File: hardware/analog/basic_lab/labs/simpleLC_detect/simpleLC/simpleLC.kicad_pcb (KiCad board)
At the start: 2 copper layers, 36.2 x 15 mm, 5 parts, among them J1 Conn_01x04_Male, J2 Conn_01x02_Male, Q2 BC547

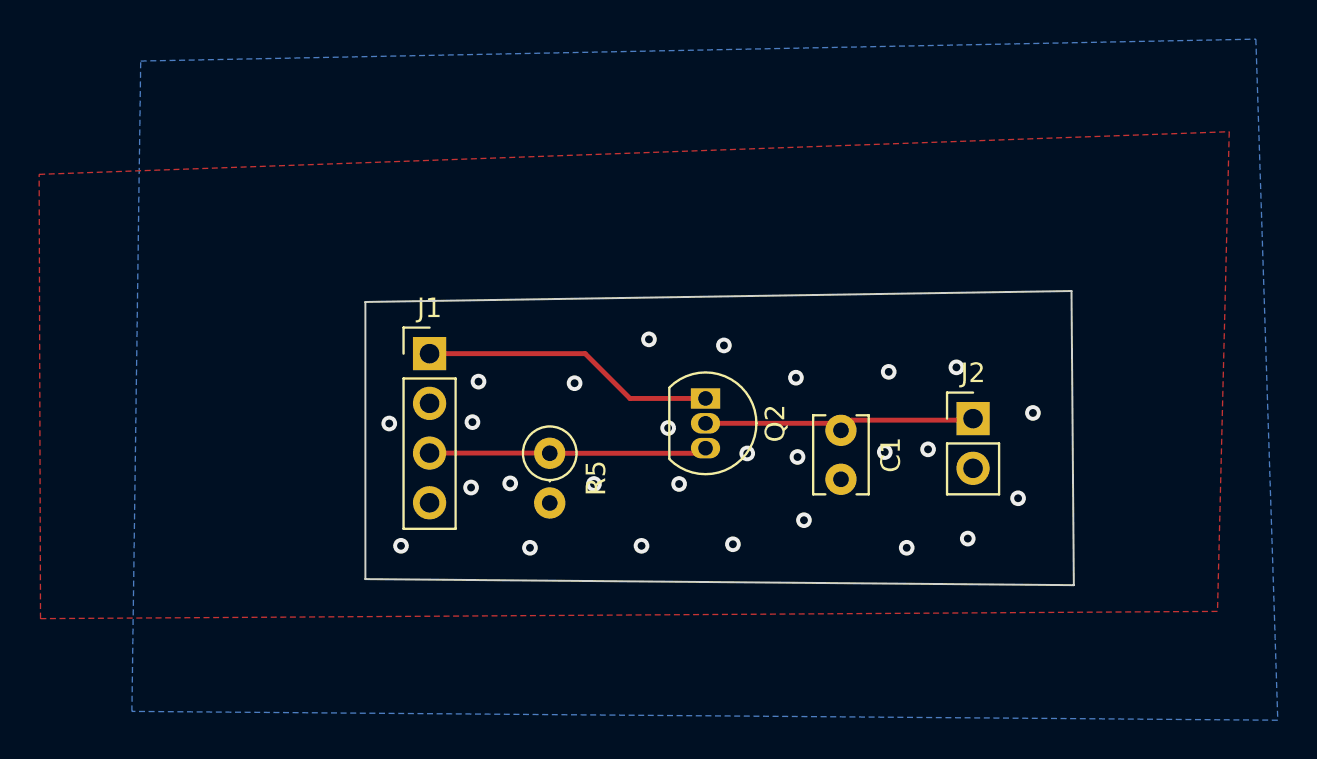
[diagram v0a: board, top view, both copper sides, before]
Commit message: PWM => detect / flyback
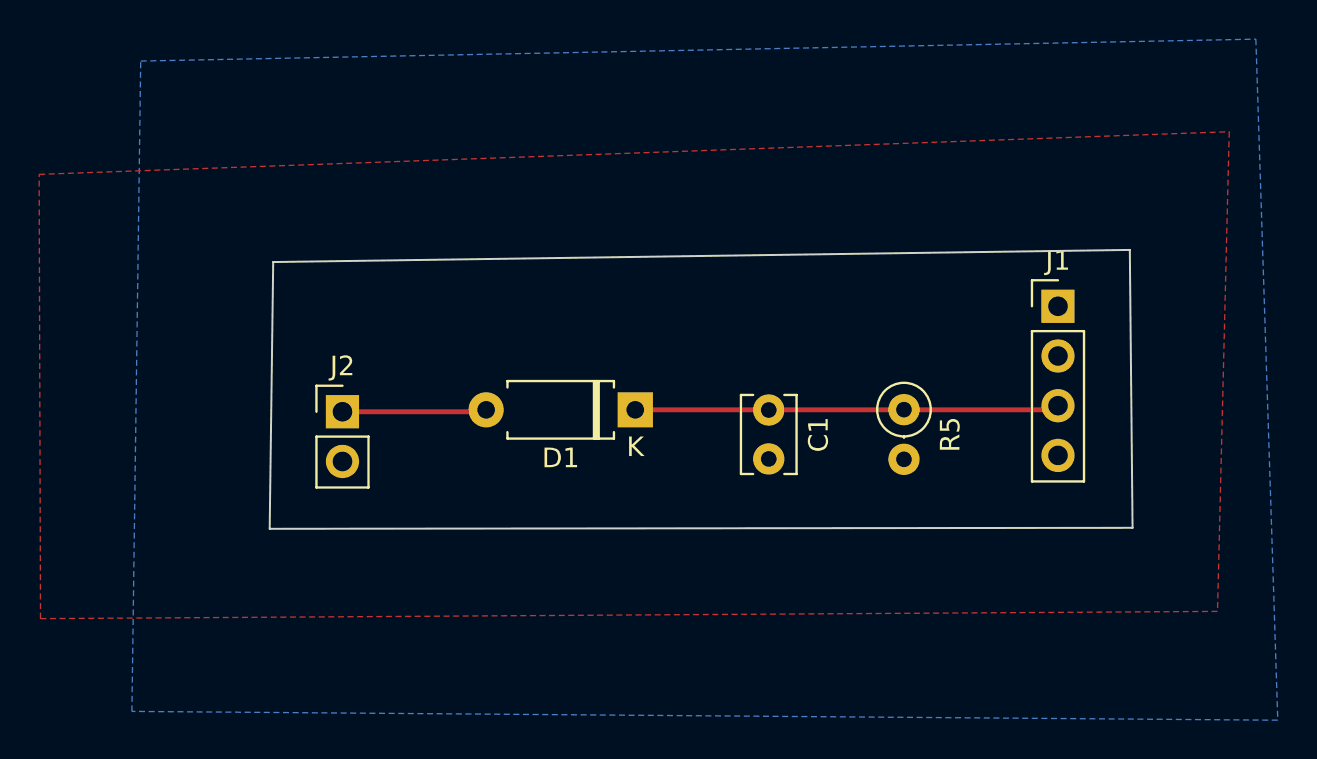
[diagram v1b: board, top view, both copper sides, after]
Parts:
- removed Q2: BC547, Package_TO_SOT_THT:TO-92_Inline
- added D1: D, Diode_THT:D_A-405_P7.62mm_Horizontal, F.Cu at (177.4, 92.5)
- moved J2 32.2 mm to (162.5, 92.7)
- moved J1 32.2 mm to (199.0, 87.3)
- moved R5 18.2 mm to (191.2, 92.5)
- moved C1 3.83 mm to (184.2, 92.6)
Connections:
- C1 pad 1: Net-(C1-Pad1) -> aout
- J2 pad 1: Net-(C1-Pad1) -> Net-(D1-Pad2)
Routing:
- net +3V3: track 15.0 -> 0.00 mm
- net Net-(C1-Pad1): track 14.0 -> 0.00 mm
- net aout: track 14.2 -> 21.8 mm
- net Net-(D1-Pad2): track 0.00 -> 7.47 mm
- net GND: vias 27 -> 0
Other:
- board size 36.2 x 15 mm -> 44.1 x 14.2 mm
